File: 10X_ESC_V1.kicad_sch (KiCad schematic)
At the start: 95 parts, among them J1 Conn_01x05_MountingPin, Q1 BUK7Y1R4-40H, Q2 BUK7Y1R4-40H, Q3 BUK7Y1R4-40H, Q4 BUK7Y1R4-40H, Q5 BUK7Y1R4-40H, Q7 BUK7Y1R4-40H, U1 STM32F051K8Ux, U2 DRV8300DPWR, U3 TPS62932, U4 TPS62932, U5 INA180B2

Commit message: D1~D3 부트스트랩 다이오드 제거 (DRV8300D 내장)
README에 있던 불필요한 다이오드 제거 완료
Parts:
- removed D1, D2, D3: D, Diode_SMD:D_SMA, symbol Device:D

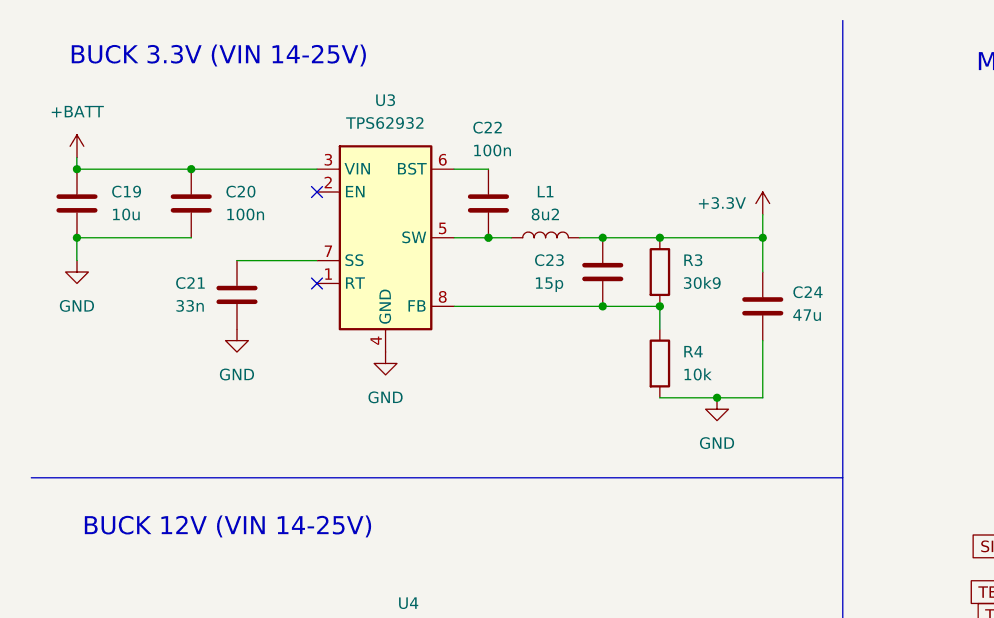
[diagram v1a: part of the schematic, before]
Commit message: 3.3V 벅 → LDO(TPS70933DBVR) 교체 및 배치
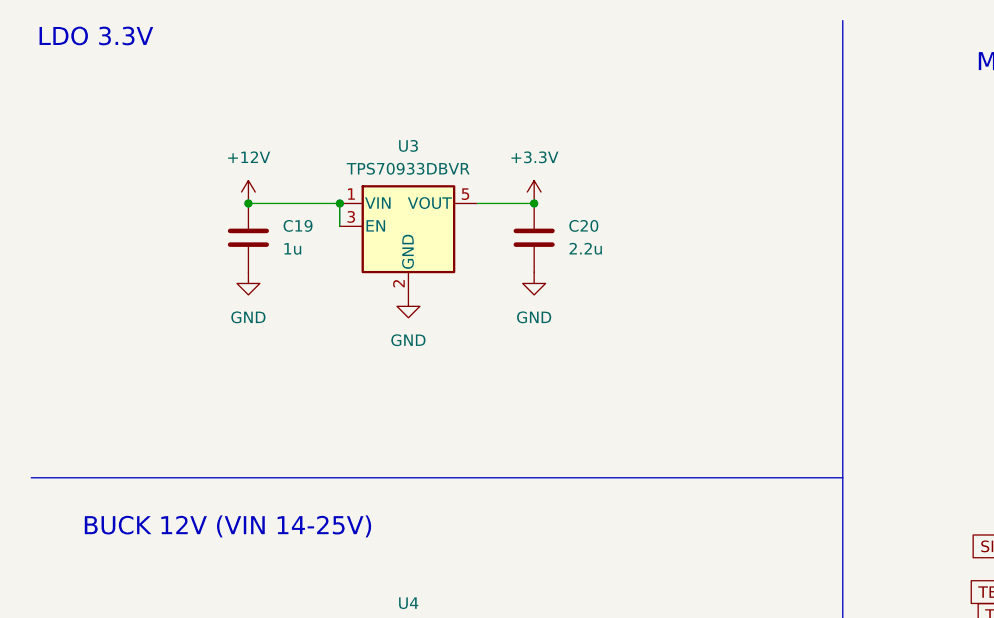
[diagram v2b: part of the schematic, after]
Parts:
- removed C21: 33n, Capacitor_SMD:C_0402_1005Metric, symbol Device:C
- removed C22: 100n, Capacitor_SMD:C_0402_1005Metric, symbol Device:C
- removed C23: 15p, Capacitor_SMD:C_0402_1005Metric, symbol Device:C
- removed C24: 47u, Capacitor_SMD:C_1210_3225Metric, symbol Device:C
- removed L1: 8u2, Inductor_SMD:L_KOHERelec_MDA7030, symbol Device:L
- removed R3: 30k9, Resistor_SMD:R_0402_1005Metric, symbol Device:R
- removed R4: 10k, Resistor_SMD:R_0402_1005Metric, symbol Device:R
- removed U3: TPS62932, Package_TO_SOT_SMD:SOT-583-8, symbol Regulator_Switching:TPS62932
- added U3: TPS70933DBVR, Package_TO_SOT_SMD:SOT-23-5, symbol Regulator_Linear:AP2112K-3.3
- C19: value 10u -> 1u; footprint Capacitor_SMD:C_0805_2012Metric -> Capacitor_SMD:C_0603_1608Metric; LCSC Part # C440198 -> (none)
- C20: value 100n -> 2.2u; LCSC Part # C14663 -> (none)
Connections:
- net +12V: now also C19.1, U3.1 (VIN), U3.3 (EN)
- net +3.3V: now also C20.1, U3.5 (VOUT)
- net +BATT: no longer C19.1, C20.1
- net GND: now also U3.2 (GND)
- no-connect marks 12 -> 10
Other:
- note added: "LDO 3.3V"
- note removed: "BUCK 3.3V (VIN 14-25V)"

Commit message: 전류 센서(U5, R12) 삭제, 로우사이드 소스 GND 직결
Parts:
- removed C28, C29: 100n, Capacitor_SMD:C_0402_1005Metric, symbol Device:C
- removed R12: 1m, Footprints:R2725, symbol Device:R
- removed R24: 1k, Resistor_SMD:R_0402_1005Metric, symbol Device:R
- removed U5: INA180B2, Package_TO_SOT_SMD:SOT-23-5, symbol Amplifier_Current:INA180B2
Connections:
- net HALF BRIDGE GND is gone; now on net GND: Q1.1 (S), Q1.2 (S), Q1.3 (S), Q2.1 (S), Q2.2 (S), Q2.3 (S), Q5.1 (S), Q5.2 (S), Q5.3 (S)
- net CURRENT: no longer U1.9 (PA3)
- no-connect marks 10 -> 11

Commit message: 개발 보드 요소 삭제 (장착구멍, LED, 테스트포인트), SWD 패드 4개로 축소
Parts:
- removed D4: LED, LED_SMD:LED_0603_1608Metric, symbol Device:LED
- removed H1, H2, H3, H4: MountingHole_Pad, Footprints:Flightcontroller_MountingHolePad_M4, symbol Mechanical:MountingHole_Pad
- removed R5: 1k5, Resistor_SMD:R_0402_1005Metric, symbol Device:R
- removed TP3: NRST, Footprints:Flightcontroller_Solder_Pad, symbol Connector:TestPoint
- removed TP6: TELEMRX, Footprints:Flightcontroller_Solder_Pad, symbol Connector:TestPoint
- removed TP7: CURRENT, Footprints:Flightcontroller_Solder_Pad, symbol Connector:TestPoint
- removed TP8: SIGNAL_INPUT, Footprints:Flightcontroller_Solder_Pad, symbol Connector:TestPoint
- removed TP9: TELEMETRY, Footprints:Flightcontroller_Solder_Pad, symbol Connector:TestPoint
- TP1, TP2, TP4, TP5: footprint Footprints:Flightcontroller_Solder_Pad -> TestPoint:TestPoint_Pad_D1.0mm
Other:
- note removed: "Mounting Holes"

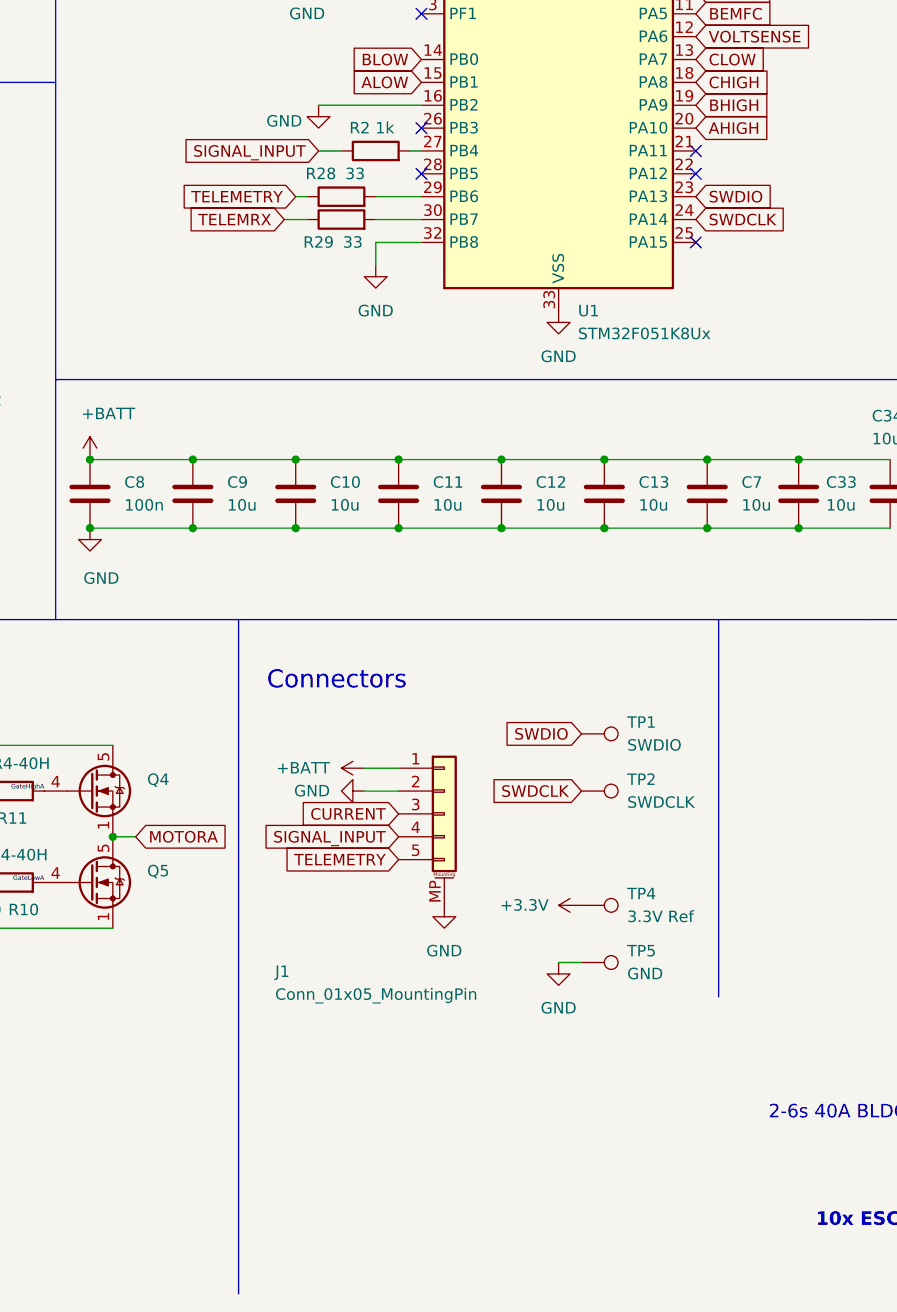
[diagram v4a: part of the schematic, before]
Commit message: J1 삭제, 배터리/모터/신호 납땜 패드 추가, 텔레메트리 제거
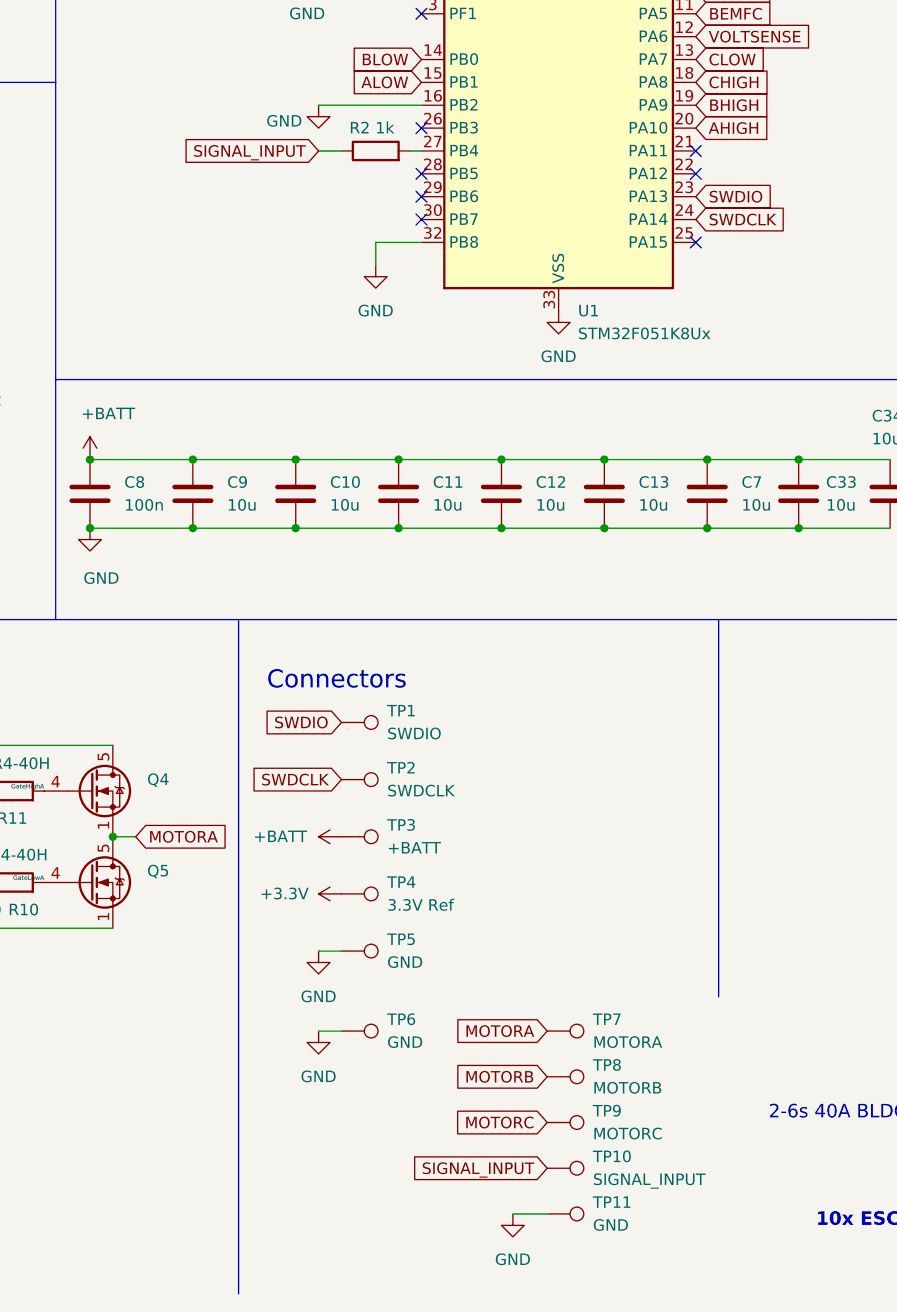
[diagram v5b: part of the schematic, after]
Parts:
- removed J1: Conn_01x05_MountingPin, Connector_JST:JST_GH_SM05B-GHS-TB_1x05-1MP_P1.25mm_Horizontal, symbol Connector_Generic_MountingPin:Conn_01x05_MountingPin
- removed R28, R29: 33, Resistor_SMD:R_0402_1005Metric, symbol Device:R
- added TP10: SIGNAL_INPUT, TestPoint:TestPoint_Pad_1.5x1.5mm, symbol Connector:TestPoint
- added TP11: GND, TestPoint:TestPoint_Pad_1.5x1.5mm, symbol Connector:TestPoint
- added TP3: +BATT, TestPoint:TestPoint_Pad_4.0x4.0mm, symbol Connector:TestPoint
- added TP6: GND, TestPoint:TestPoint_Pad_4.0x4.0mm, symbol Connector:TestPoint
- added TP7: MOTORA, TestPoint:TestPoint_Pad_4.0x4.0mm, symbol Connector:TestPoint
- added TP8: MOTORB, TestPoint:TestPoint_Pad_4.0x4.0mm, symbol Connector:TestPoint
- added TP9: MOTORC, TestPoint:TestPoint_Pad_4.0x4.0mm, symbol Connector:TestPoint
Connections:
- net +BATT: now also TP3.1
- net GND: now also TP11.1, TP6.1
- net MOTORA: now also TP7.1
- net MOTORB: now also TP8.1
- net MOTORC: now also TP9.1
- net SIGNAL_INPUT: now also TP10.1
- no-connect marks 11 -> 13

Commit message: V2 배치 완료: 36x21 양면, 납땜 패드 배치
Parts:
- TP3, TP6: footprint TestPoint:TestPoint_Pad_4.0x4.0mm -> TestPoint:TestPoint_Pad_3.0x3.0mm
- TP7, TP8, TP9: footprint TestPoint:TestPoint_Pad_4.0x4.0mm -> TestPoint:TestPoint_Pad_2.5x2.5mm
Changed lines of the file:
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@@
 			)
 		)
-		(property "Footprint" "TestPoint:TestPoint_Pad_4.0x4.0mm"
+		(property "Footprint" "TestPoint:TestPoint_Pad_2.5x2.5mm"
 			(at 157.48 184.15 0)
 			(hide yes)
@@
 			)
 		)
-		(property "Footprint" "TestPoint:TestPoint_Pad_4.0x4.0mm"
+		(property "Footprint" "TestPoint:TestPoint_Pad_2.5x2.5mm"
 			(at 157.48 173.99 0)
 			(hide yes)
@@
 			)
 		)
-		(property "Footprint" "TestPoint:TestPoint_Pad_4.0x4.0mm"
+		(property "Footprint" "TestPoint:TestPoint_Pad_2.5x2.5mm"
 			(at 157.48 179.07 0)
 			(hide yes)
@@
 			)
 		)
-		(property "Footprint" "TestPoint:TestPoint_Pad_4.0x4.0mm"
+		(property "Footprint" "TestPoint:TestPoint_Pad_3.0x3.0mm"
 			(at 134.62 173.99 0)
 			(hide yes)
@@
 			)
 		)
-		(property "Footprint" "TestPoint:TestPoint_Pad_4.0x4.0mm"
+		(property "Footprint" "TestPoint:TestPoint_Pad_3.0x3.0mm"
 			(at 134.62 152.4 0)
 			(hide yes)
